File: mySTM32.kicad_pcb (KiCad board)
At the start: 2 copper layers, 138 x 108 mm, 122 parts, among them J1 conn1X2, J10 DB9_Female****, J11 USB_OTG, J12 conn2X16, J13 conn2X3, J14 Conn_02x02, J15 conn2X3, J16 conn1X2, J17 conn2X2, J18 JTAG, J19 Conn_02x17_Odd_Even, J2 USB_OTG, J20 Conn_02x22_Odd_Even, J21 conn2X9, J22 conn2X3, J23 Conn2x4, J3 conn2X3, J4 conn2X2, J5 conn2X2, J6 conn1X2, J7 Conn_01x02, J8 Conn2x4, J9 conn2X4, Q1 Q_NPN_BEC(S8050), Q2 Q_NPN_BEC, Q3 Q_NPN_BEC(S8050), SW1 KFT8.0, SW2 WAKUP, SW3 RESET, SW4 KE1, SW5 KEY2, U1 AT24C02, U2 W25Q16, U3 SD-Card, U4 SP3485, U5 SN65HVD230, U6 CH340G, U7 AMS1117, U8 SP3232, U9 STM32F103VET6, Y1 12MHz, Y2 32.768KHz, Y3 8MHz

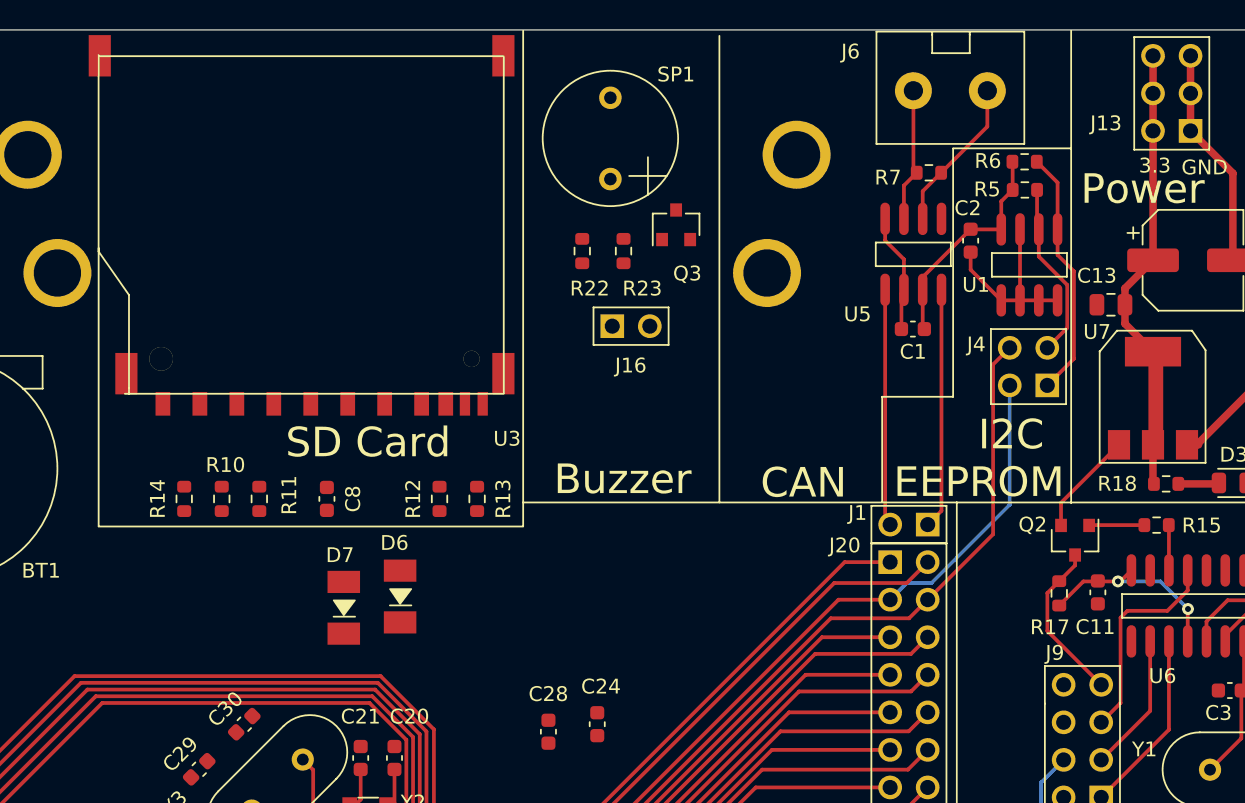
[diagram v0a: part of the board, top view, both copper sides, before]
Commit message: [buzzer, lib] [layout] SD-Card
Signed-off-by: EasonLiang <liangyx25@163.com>
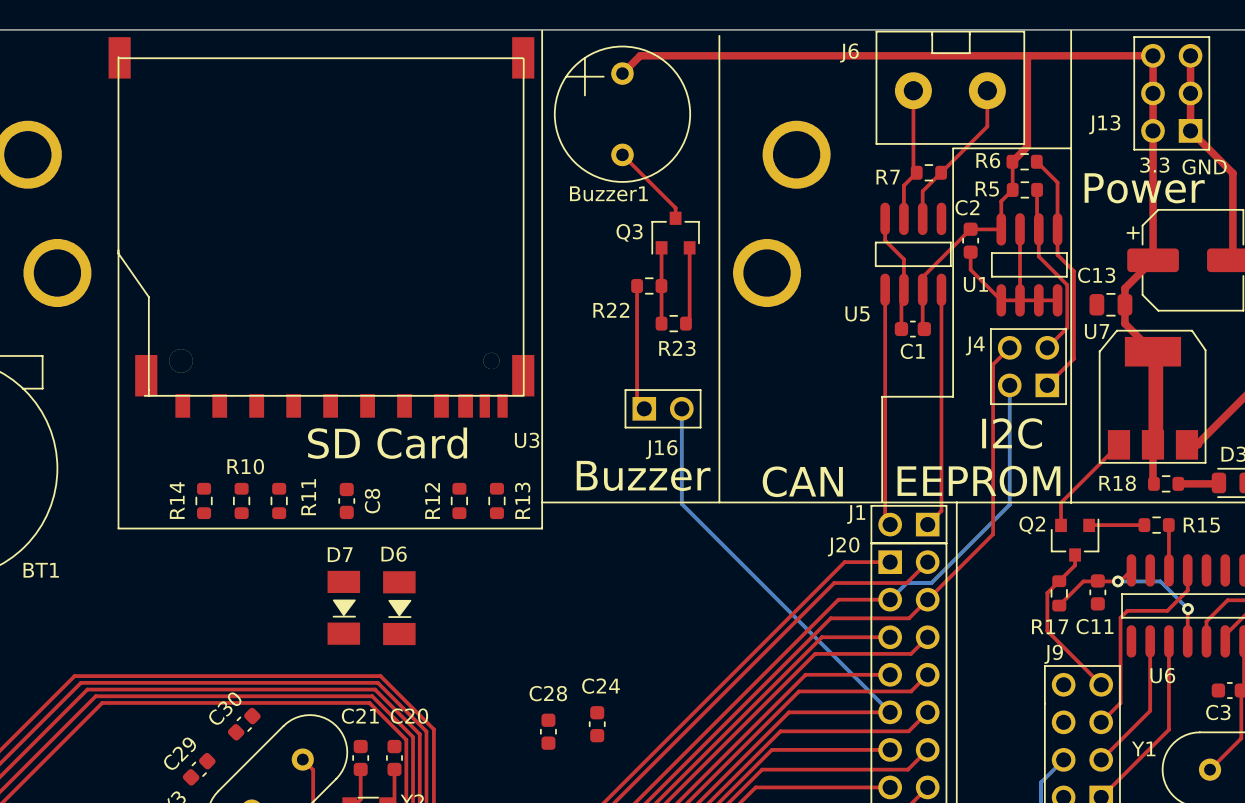
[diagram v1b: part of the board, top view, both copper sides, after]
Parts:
- removed SP1: Speaker, mypcb:BEEP9X5.5
- added Buzzer1: Speaker, mypcb:BEEP9X5.5, F.Cu at (111.4, 35.7)
- moved J16 5.99 mm to (114.2, 55.6)
- moved R23 5.97 mm to (114.9, 49.9), turned to 0 degrees
- moved R22 5.11 mm to (113.2, 47.3), turned to 0 degrees
- moved U3 1.35 mm to (104.7, 31.9)
- moved C8 1.35 mm to (92.8, 61.9)
- moved R10 1.35 mm to (85.7, 61.9)
- moved R11 1.35 mm to (88.2, 61.9)
- moved R12 1.35 mm to (100.4, 61.9)
- moved R13 1.35 mm to (102.9, 61.9)
- moved R14 1.35 mm to (83.1, 61.9)
- moved D6 0.79 mm to (96.3, 69.1)
- moved Q3 0.56 mm to (115.0, 43.7)
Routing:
- net +3V3: track 67.4 -> 111.3 mm
- net /BEEP: track 28.5 -> 54.9 mm
- net Net-(J16-Pad1): track 0.00 -> 8.51 mm
- net Net-(Buzzer1-Pad2): track 0.00 -> 5.78 mm
- net GND: track 69.3 -> 74.6 mm
- net Net-(Q3-Pad1): track 0.00 -> 5.13 mm

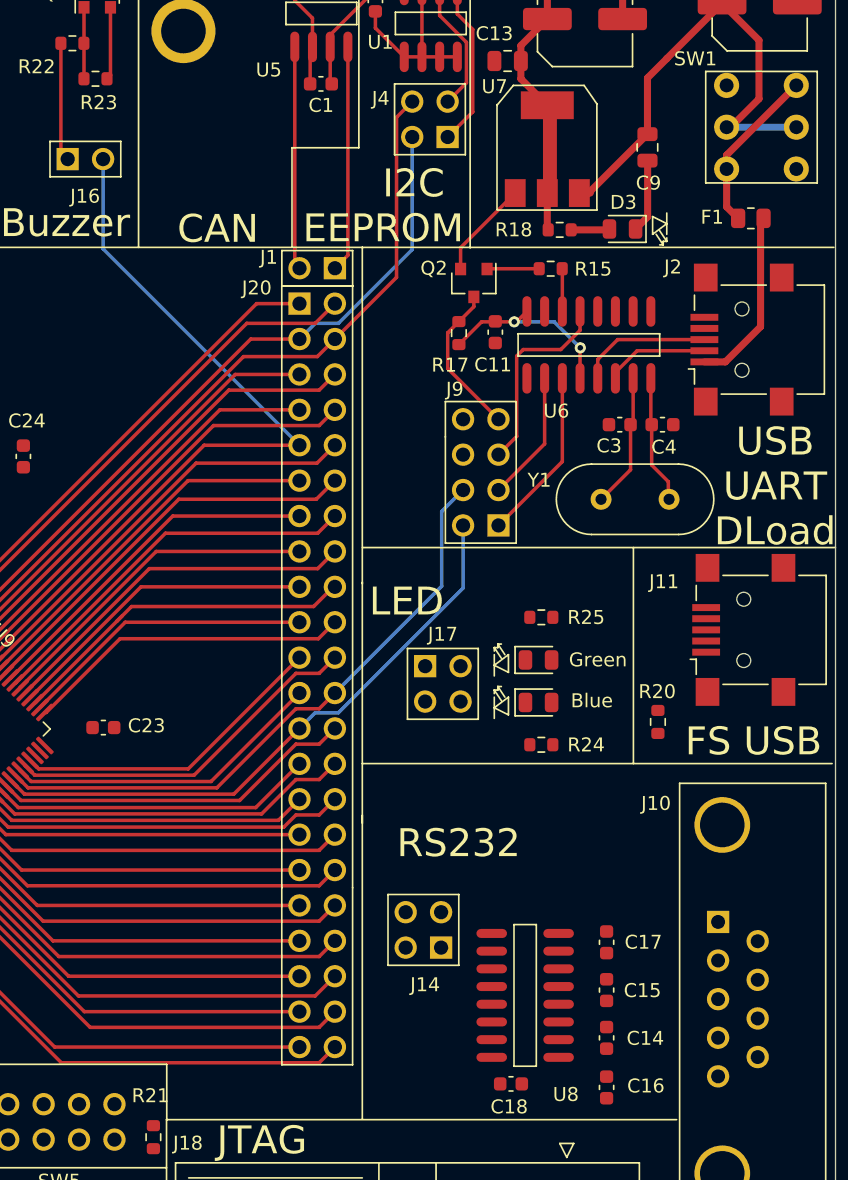
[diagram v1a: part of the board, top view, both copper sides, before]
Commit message: [FS USB]	[LED]	[Conn Annotation]
Signed-off-by: EasonLiang <liangyx25@163.com>
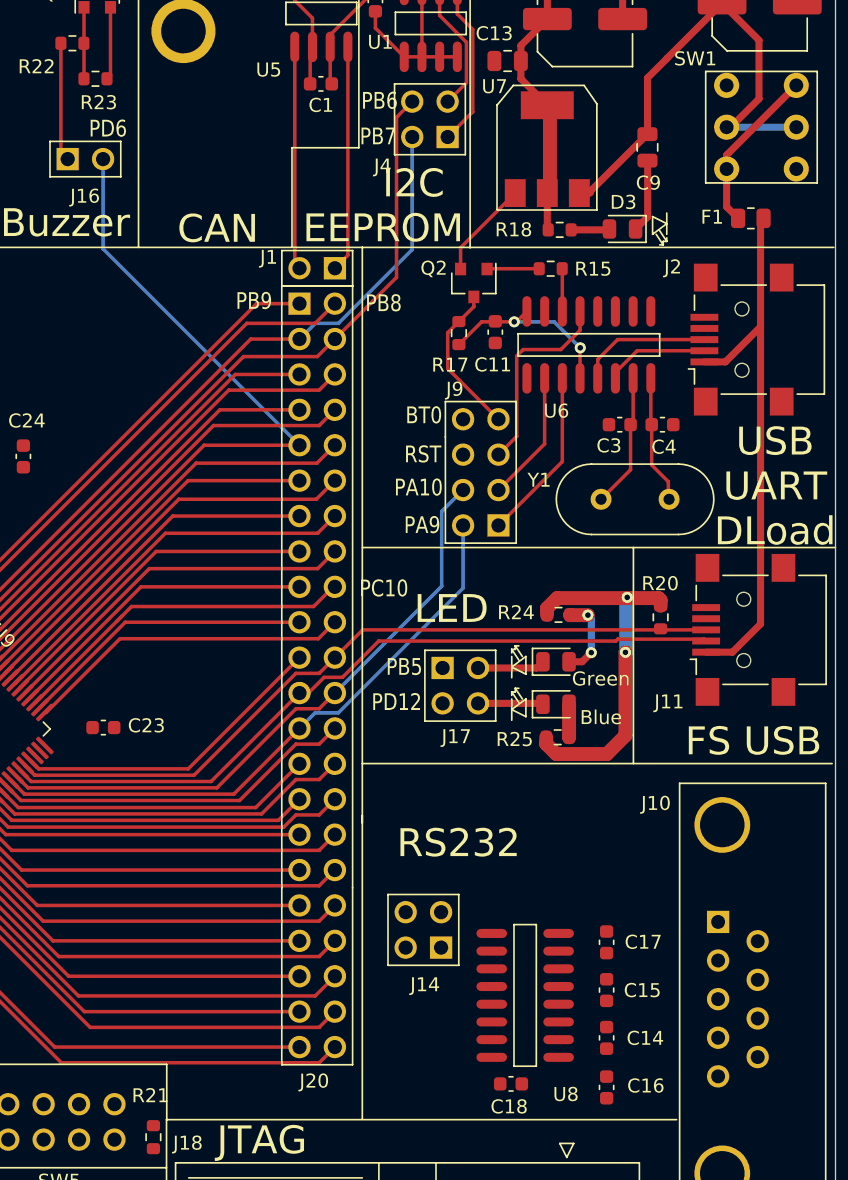
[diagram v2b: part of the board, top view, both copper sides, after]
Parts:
- moved R24 9.40 mm to (148.1, 88.3)
- moved R25 8.69 mm to (148.1, 97.1)
- moved R20 7.51 mm to (155.5, 88.5), turned to 270 degrees
- moved D4 1.26 mm to (147.9, 91.7)
- moved D5 1.26 mm to (147.9, 94.7)
- moved J17 1.26 mm to (141.1, 92.1)
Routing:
- net /PA11: track 23.0 -> 53.9 mm
- net /PA12: track 26.0 -> 53.5 mm
- net +3V3: track 111.3 -> 137.6 mm, vias 2 -> 4
- net +5V: track 12.6 -> 38.7 mm
- net Net-(D4-Pad2): track 0.00 -> 5.95 mm, vias 0 -> 2
- net Net-(D4-Pad1): track 0.00 -> 4.84 mm
- net Net-(D5-Pad1): track 0.00 -> 4.68 mm
- net Net-(D5-Pad2): track 0.00 -> 2.37 mm
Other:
- board text added: "BT0"
- board text added: "PA10"
- board text added: "PA9"
- board text added: "PB5"
- board text added: "PB6"
- board text added: "PB7"
- board text added: "PB8"
- board text added: "PB9"
- board text added: "PC10"
- board text added: "PD12"
- board text added: "PD6"
- board text added: "RST"

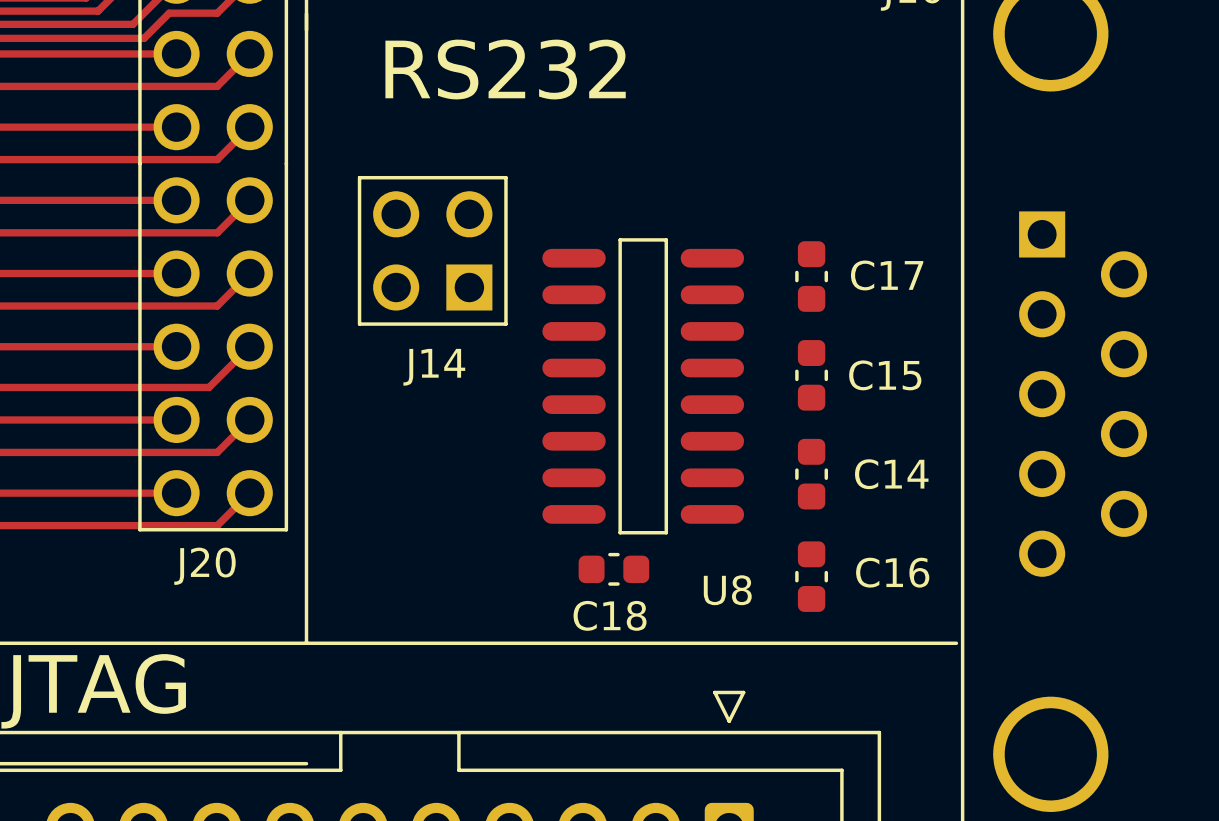
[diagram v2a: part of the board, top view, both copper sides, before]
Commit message: [RS232]
Signed-off-by: EasonLiang <liangyx25@163.com>
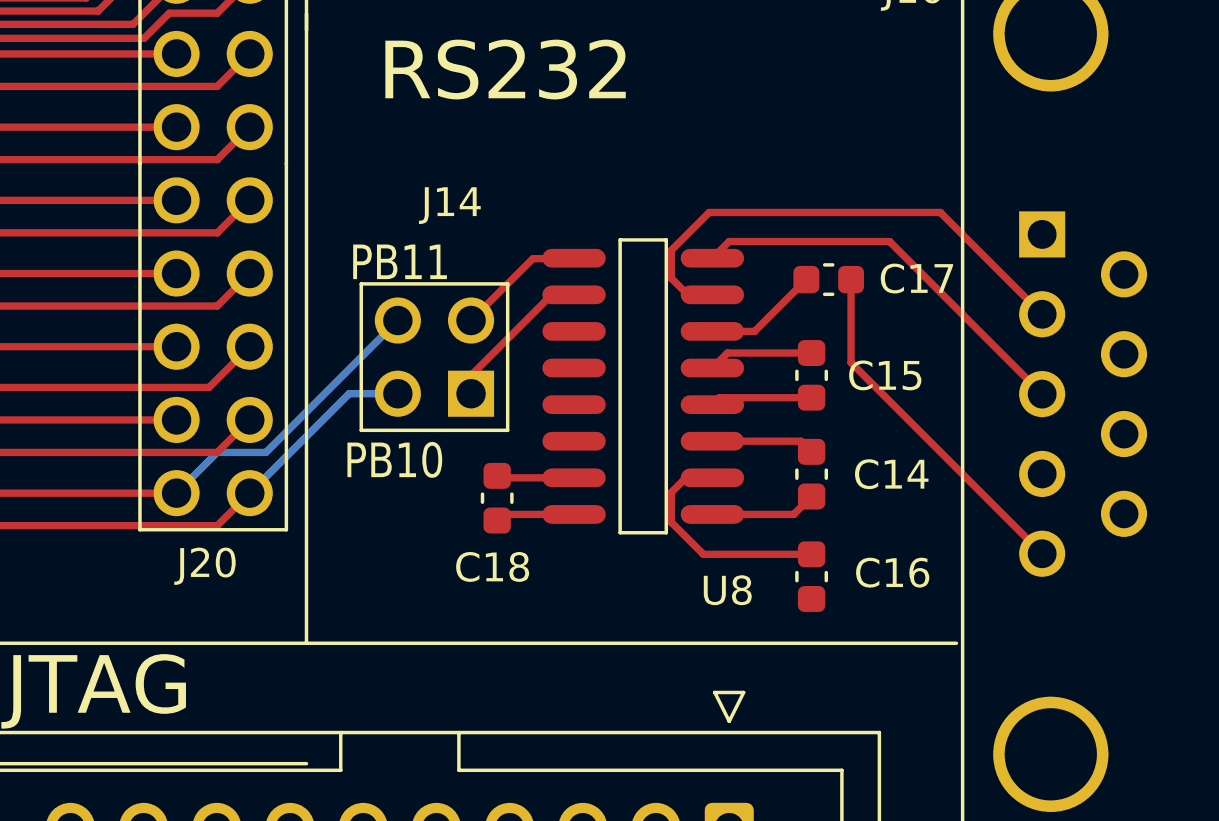
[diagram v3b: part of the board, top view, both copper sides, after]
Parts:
- moved C18 4.74 mm to (140.7, 119.5), turned to 270 degrees
- moved J14 3.69 mm to (138.5, 115.9)
- moved C17 0.60 mm to (152.2, 111.9), turned to 0 degrees
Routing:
- net Net-(J10-Pad2): track 0.00 -> 17.5 mm
- net GND: track 74.6 -> 89.5 mm
- net Net-(J10-Pad3): track 0.00 -> 13.9 mm
- net /PB11: track 37.0 -> 47.2 mm
- net Net-(C16-Pad1): track 0.00 -> 8.00 mm
- net /PB10: track 41.4 -> 48.0 mm
- net Net-(J14-Pad1): track 0.00 -> 5.37 mm
- net Net-(J14-Pad3): track 0.00 -> 4.48 mm
- net Net-(C17-Pad1): track 0.00 -> 4.01 mm
- net Net-(C14-Pad2): track 0.00 -> 3.70 mm
- net Net-(C15-Pad1): track 0.00 -> 3.66 mm
- net Net-(C14-Pad1): track 0.00 -> 3.59 mm
- net Net-(C15-Pad2): track 0.00 -> 3.54 mm
- net +3V3: track 137.6 -> 140.4 mm
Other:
- board text added: "PB10"
- board text added: "PB11"
